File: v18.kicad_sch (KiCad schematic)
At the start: 62 parts, among them U51 ADP5071ACPZ, U52 TPS7A4700xRGW, U53 TPS7A3301RGW

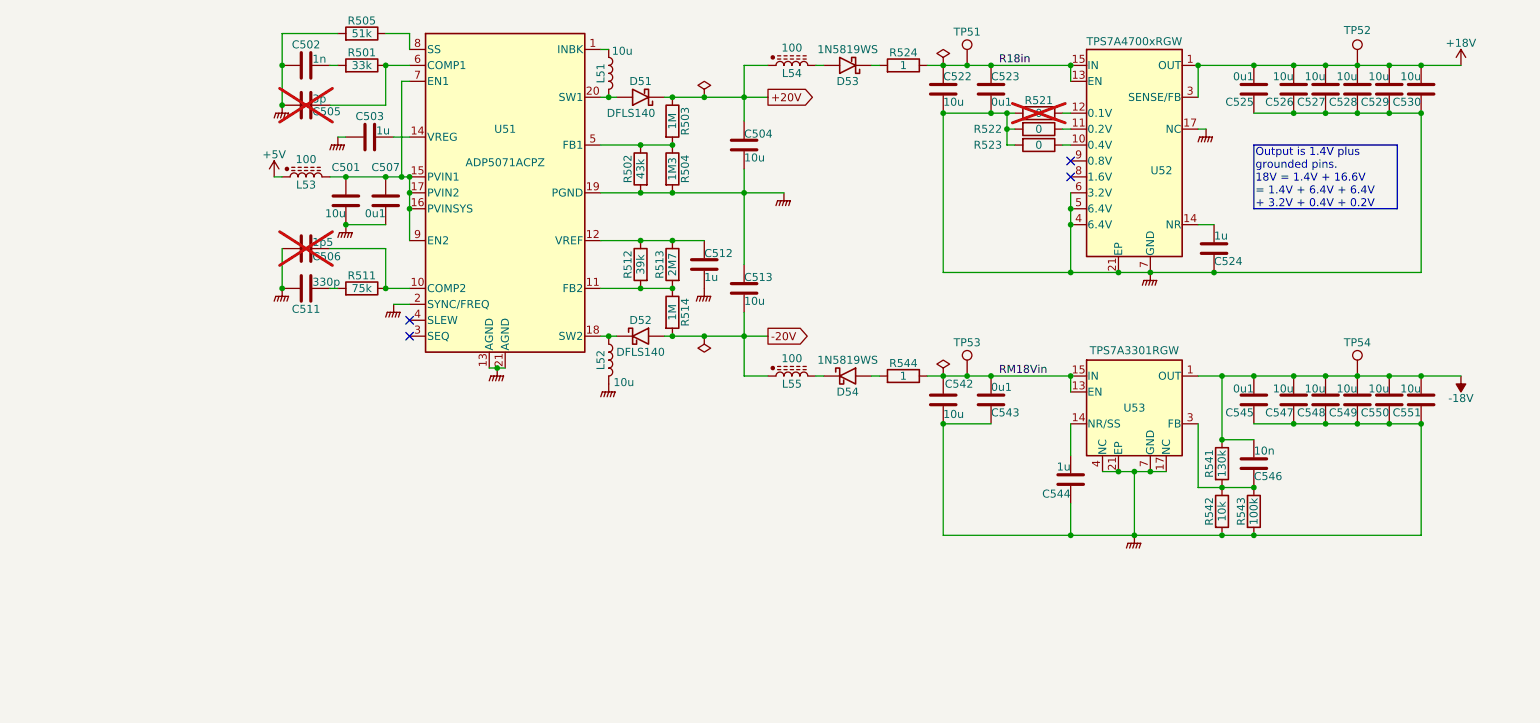
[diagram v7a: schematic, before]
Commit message: Layout underway
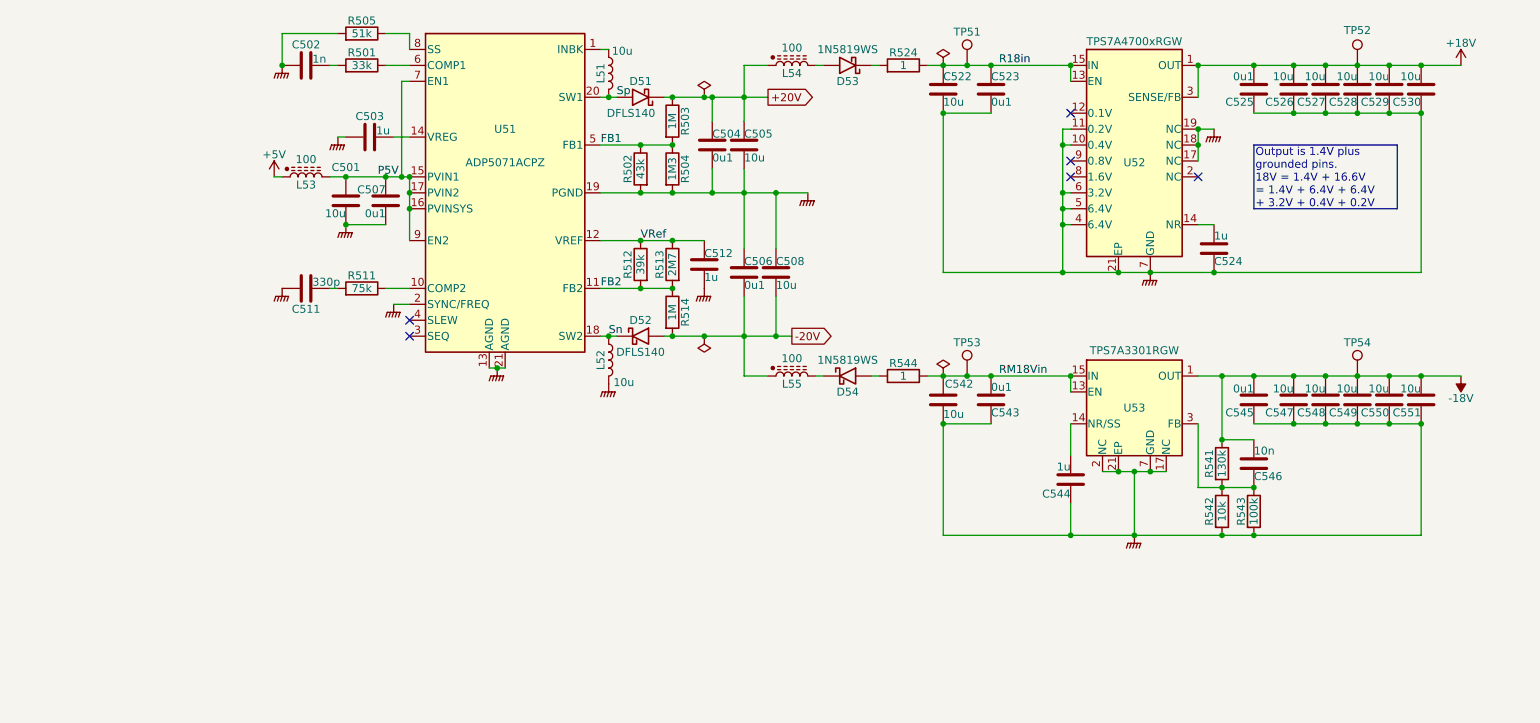
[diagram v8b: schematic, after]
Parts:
- removed C505: 3p, Capacitor_SMD:C_0603_1608Metric, symbol Device:C
- removed R521, R522, R523: 0, Resistor_SMD:R_0603_1608Metric, symbol Device:R
- added C504: 0u1, Capacitor_SMD:C_0402_1005Metric, symbol Device:C
- C506: value 1p5 -> 0u1; footprint Capacitor_SMD:C_0603_1608Metric -> Capacitor_SMD:C_0402_1005Metric; LCSC (none) -> C307331; now fitted; now in the parts list
- U52, U53: footprint Package_DFN_QFN:Texas_RGW0020A_VQFN-20-1EP_5x5mm_P0.65mm_EP3.15x3.15mm_ThermalVias -> Package_DFN_QFN:Texas_RGW0020A_VQFN-20-1EP_5x5mm_P0.65mm_EP3.15x3.15mm
- renumbered C504 to C505, C513 to C508
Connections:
- net +20V: now also C504.2
- net -20V: now also C506.1
- net GNDPWR: now also C506.2, U52.10 (0.4V), U52.11 (0.2V), U53.2 (NC), C504.1; no longer C506.1
- net FB1: now reaches R502.1, R503.2, R504.1, U51.5 (FB1)
- net VRef: now reaches C512.1, R512.1, R513.1, U51.12 (VREF)
- net FB2: now reaches R512.2, R513.2, R514.1, U51.11 (FB2)
- net at R511.1, U51.10 (COMP2): no longer C506.2
- net P5V: now reaches C501.1, C507.2, L53.2, U51.15 (PVIN1), U51.16 (PVINSYS), U51.17 (PVIN2), U51.7 (EN1), U51.9 (EN2)
- net Sn: now reaches D52.1 (K), L52.1, U51.18 (SW2)
- net Sp: now reaches D51.2 (A), L51.2, U51.20 (SW1)
- no-connect marks 4 -> 6
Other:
- moved on the sheet: C508
